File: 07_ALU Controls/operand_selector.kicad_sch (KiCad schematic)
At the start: 1 part, among them U3 74LS139

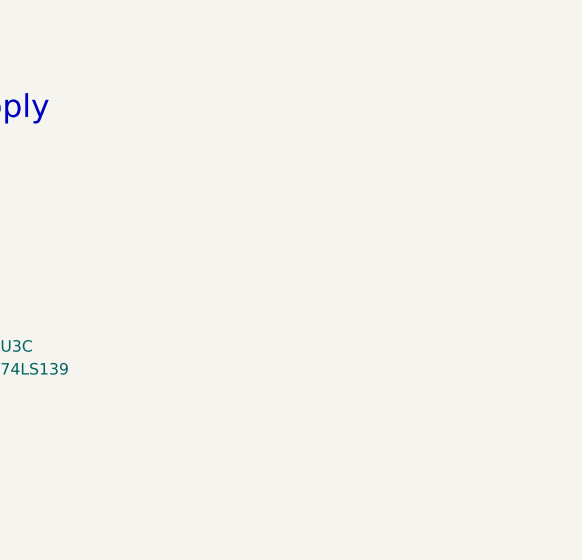
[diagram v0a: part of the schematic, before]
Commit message: Last revision of the cpu, all boards have been ordered. Implementation to be tested and documented in following commits.
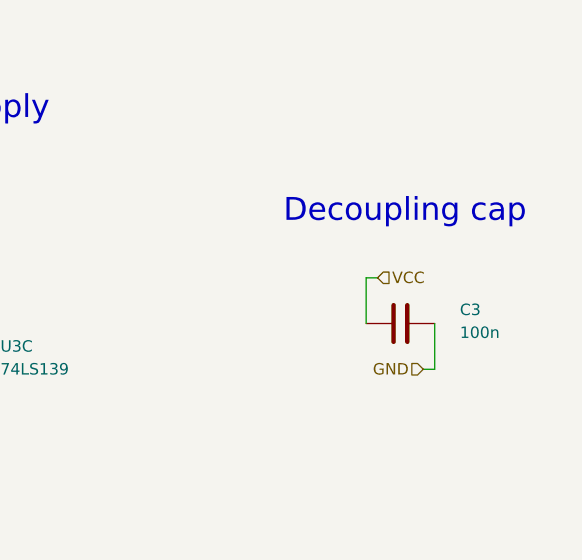
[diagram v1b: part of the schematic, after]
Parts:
- added C3: 100n, Capacitor_THT:C_Disc_D3.0mm_W1.6mm_P2.50mm, symbol Device:C
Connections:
- net GND: now also C3.2
- net VCC: now also C3.1
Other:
- note added: "Decoupling cap"
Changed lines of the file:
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@@
+		)
+	)
+	(text "Decoupling cap"
+		(exclude_from_sim no)
+		(at 222.758 76.454 0)
+		(effects
+			(font
+				(size 2.54 2.54)
+			)
 		)
 	)
@@
 	(wire
 		(pts
+			(xy 219.71 83.82) (xy 218.44 83.82)
+		)
+		(stroke
+			(width 0)
+			(type default)
+		)
+	)
+	(wire
+		(pts
 			(xy 93.98 77.47) (xy 96.52 77.47)
 		)
@@
 	(wire
 		(pts
+			(xy 224.79 93.98) (xy 226.06 93.98)
+		)
+		(stroke
+			(width 0)
+			(type default)
+		)
+	)
+	(wire
+		(pts
+			(xy 226.06 88.9) (xy 226.06 93.98)
+		)
+		(stroke
+			(width 0)
+			(type default)
+		)
+	)
+	(wire
+		(pts
 			(xy 124.46 80.01) (xy 121.92 80.01)
 		)
@@
 		)
 	)
+	(wire
+		(pts
+			(xy 218.44 83.82) (xy 218.44 88.9)
+		)
+		(stroke
+			(width 0)
+			(type default)
+		)
+	)
 	(hierarchical_label "YC0"
 		(shape input)
@@
 		)
 	)
+	(hierarchical_label "GND"
+		(shape input)
+		(at 224.79 93.98 180)
+		(effects
+			(font
+				(size 1.27 1.27)
+			)
+			(justify right)
+		)
+	)
 	(hierarchical_label "YC1"
 		(shape input)
@@
 			)
 			(justify right)
+		)
+	)
+	(hierarchical_label "VCC"
+		(shape input)
+		(at 219.71 83.82 0)
+		(effects
+			(font
+				(size 1.27 1.27)
+			)
+			(justify left)
 		)
 	)
@@
 				)
 			)
+		)
+	)
+	(symbol
+		(lib_id "Device:C")
+		(at 222.25 88.9 90)
+		(unit 1)
+		(exclude_from_sim no)
+		(in_bom yes)
+		(on_board yes)
+		(dnp no)
+		(property "Reference" "C3"
+			(at 228.854 87.376 90)
+			(effects
+				(font
+					(size 1.27 1.27)
+				)
+				(justify right)
+			)
+		)
+		(property "Value" "100n"
+			(at 228.854 89.916 90)
+			(effects
+				(font
+					(size 1.27 1.27)
+				)
+				(justify right)
+			)
+		)
+		(property "Footprint" "Capacitor_THT:C_Disc_D3.0mm_W1.6mm_P2.50mm"
+			(at 226.06 87.9348 0)
+			(effects
+				(font
+					(size 1.27 1.27)
+				)
+				(hide yes)
+			)
+		)
+		(property "Datasheet" "~"
+			(at 222.25 88.9 0)
+			(effects
+				(font
+					(size 1.27 1.27)
+				)
+				(hide yes)
+			)
+		)
+		(property "Description" "Unpolarized capacitor"
+			(at 222.25 88.9 0)
+			(effects
+				(font
+					(size 1.27 1.27)
+				)
+				(hide yes)
+			)
+		)
+		(pin "2"
+		)
+		(pin "1"
+		)
+		(instances
+			(project "ALU Controls"
+				(path "/467f3bd9-3b72-47f3-8962-bc0cb708391a/9f681643-045f-45cc-b43e-c78c303ca585"
+					(reference "C3")
+					(unit 1)
+				)
+			)
